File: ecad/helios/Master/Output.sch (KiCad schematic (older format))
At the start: 26 parts, among them J5 MCV 1,5/ 2-G-3,81, J6 MiniFit JR 5556 08A2, Q1 IRF9Z34NPbF, Q2 BSS84P, U2 STEF01FTR, U3 ISO7320FC, U4 UA9638

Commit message: Corrects anotation of Helios Master
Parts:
- D3, D4: value CPDT-5V0-HF -> CPDT-5V0USP-HF; Part Number CPDT-5V0-HF -> CPDT-5V0USP-HF
- renumbered R7 to R13, U4 to U7, U3 to U9
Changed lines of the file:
@@
 V36
 $Comp
-L master-rescue:ISO7320FC U3
+L master-rescue:ISO7320FC U9
 U 1 1 5AC3E36A
 P 2900 4100
-AR Path="/5AC39A79/5AC3E36A" Ref="U3"  Part="1"
+AR Path="/5AC39A79/5AC3E36A" Ref="U9"  Part="1"
 AR Path="/5AC440F9/5AC3E36A" Ref="U5"  Part="1"
 AR Path="/5AC443F1/5AC3E36A" Ref="U10"  Part="1"
 AR Path="/5AC443F5/5AC3E36A" Ref="U15"  Part="1"
-F 0 "U3" H 2900 4525 50  0000 C CNN
+F 0 "U9" H 2900 4525 50  0000 C CNN
 F 1 "ISO7320FC" H 2900 4450 50  0000 C CNN
 F 2 "Package_SO:SOIC-8_3.9x4.9mm_P1.27mm" H 2900 3750 50  0001 C CIN
@@
 $EndComp
 $Comp
-L master-rescue:UA9638 U4
+L master-rescue:UA9638 U7
 U 1 1 5AC3EEA4
 P 5750 4100
-AR Path="/5AC39A79/5AC3EEA4" Ref="U4"  Part="1"
+AR Path="/5AC39A79/5AC3EEA4" Ref="U7"  Part="1"
 AR Path="/5AC440F9/5AC3EEA4" Ref="U6"  Part="1"
 AR Path="/5AC443F1/5AC3EEA4" Ref="U11"  Part="1"
 AR Path="/5AC443F5/5AC3EEA4" Ref="U16"  Part="1"
-F 0 "U4" H 5600 4200 50  0000 C CNN
+F 0 "U7" H 5600 4200 50  0000 C CNN
 F 1 "UA9638" H 5650 4100 50  0000 C CNN
 F 2 "Package_SO:SOIC-8_3.9x4.9mm_P1.27mm" H 5750 4100 50  0001 C CNN
@@
 $EndComp
 $Comp
-L master-rescue:UA9638 U4
+L master-rescue:UA9638 U7
 U 2 1 5AC3EF24
 P 5750 5250
-AR Path="/5AC39A79/5AC3EF24" Ref="U4"  Part="2"
+AR Path="/5AC39A79/5AC3EF24" Ref="U7"  Part="2"
 AR Path="/5AC440F9/5AC3EF24" Ref="U6"  Part="2"
 AR Path="/5AC443F1/5AC3EF24" Ref="U11"  Part="2"
 AR Path="/5AC443F5/5AC3EF24" Ref="U16"  Part="2"
-F 0 "U4" H 5600 5350 50  0000 C CNN
+F 0 "U7" H 5600 5350 50  0000 C CNN
 F 1 "UA9638" H 5700 5250 50  0000 C CNN
 F 2 "Package_SO:SOIC-8_3.9x4.9mm_P1.27mm" H 5750 5250 50  0001 C CNN
@@
 $EndComp
 $Comp
-L master-rescue:R R7
+L master-rescue:R R13
 U 1 1 5B3E59CE
 P 10150 1850
-AR Path="/5AC39A79/5B3E59CE" Ref="R7"  Part="1"
+AR Path="/5AC39A79/5B3E59CE" Ref="R13"  Part="1"
 AR Path="/5AC440F9/5B3E59CE" Ref="R14"  Part="1"
 AR Path="/5AC443F1/5B3E59CE" Ref="R27"  Part="1"
 AR Path="/5AC443F5/5B3E59CE" Ref="R34"  Part="1"
-F 0 "R7" V 10230 1850 50  0000 C CNN
+F 0 "R13" V 10230 1850 50  0000 C CNN
 F 1 "10K" V 10150 1850 50  0000 C CNN
 F 2 "Resistor_SMD:R_0603_1608Metric" V 10080 1850 50  0001 C CNN
@@
 AR Path="/5AC443F1/5B3E9AF8" Ref="R26"  Part="1"
 AR Path="/5AC443F5/5B3E9AF8" Ref="R33"  Part="1"
-AR Path="/5AC39A79/5B3E9AF8" Ref="R6"  Part="1"
-F 0 "R6" V 8880 1800 50  0000 C CNN
+AR Path="/5AC39A79/5B3E9AF8" Ref="R12"  Part="1"
+F 0 "R12" V 8880 1800 50  0000 C CNN
 F 1 "100K" V 8800 1800 50  0000 C CNN
 F 2 "Resistor_SMD:R_0603_1608Metric" V 8730 1800 50  0001 C CNN
@@
 P 6850 4550
 F 0 "D3" H 6850 4766 50  0000 C CNN
-F 1 "CPDT-5V0-HF" H 6850 4675 50  0000 C CNN
+F 1 "CPDT-5V0USP-HF" H 6850 4675 50  0000 C CNN
 F 2 "Package_TO_SOT_SMD:SOT-23" H 6700 4550 50  0001 C CNN
 F 3 "~" H 6700 4550 50  0001 C CNN
-F 4 "CPDT-5V0-HF" H 6850 4550 50  0001 C CNN "Part Number"
+F 4 "CPDT-5V0USP-HF" H 6850 4550 50  0001 C CNN "Part Number"
 	1    6850 4550
 	1    0    0    -1
@@
 P 6850 5700
 F 0 "D4" H 6850 5916 50  0000 C CNN
-F 1 "CPDT-5V0-HF" H 6850 5825 50  0000 C CNN
+F 1 "CPDT-5V0USP-HF" H 6850 5825 50  0000 C CNN
 F 2 "Package_TO_SOT_SMD:SOT-23" H 6700 5700 50  0001 C CNN
 F 3 "~" H 6700 5700 50  0001 C CNN
-F 4 "CPDT-5V0-HF" H 6850 5700 50  0001 C CNN "Part Number"
+F 4 "CPDT-5V0USP-HF" H 6850 5700 50  0001 C CNN "Part Number"
 	1    6850 5700
 	1    0    0    -1

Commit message: Updates board for manufacturing
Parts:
- C2, C3: value 47uF, 50V -> (none)
- C45, C5, C6, C7: value 100nF -> 100n; Part Number 06035C104KAT2A -> CC0603KRX7R8BB104
- J6: value MiniFit JR 5556 08A2 -> MiniFit JR 5566 08A2
- Q1: footprint Package_TO_SOT_THT:TO-220-3_Horizontal_TabDown -> Package_TO_SOT_THT:TO-220-3_Vertical
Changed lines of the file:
@@
 F 0 "Q1" H 2600 1450 50  0000 L CNN
 F 1 "IRF9Z34NPbF" H 2600 1350 50  0000 L CNN
-F 2 "Package_TO_SOT_THT:TO-220-3_Horizontal_TabDown" H 2600 1500 50  0001 C CNN
+F 2 "Package_TO_SOT_THT:TO-220-3_Vertical" H 2600 1500 50  0001 C CNN
 F 3 "" H 2400 1400 50  0001 C CNN
 F 4 "IRF9Z34NPbF" H 2400 1400 60  0001 C CNN "Part Number"
@@
 AR Path="/5AC443F5/5AC3EBB4" Ref="C29"  Part="1"
 F 0 "C7" H 3575 3900 50  0000 L CNN
-F 1 "100nF" H 3575 3700 50  0000 L CNN
+F 1 "100n" H 3575 3700 50  0000 L CNN
 F 2 "Capacitor_SMD:C_0603_1608Metric" H 3588 3650 50  0001 C CNN
 F 3 "" H 3550 3800 50  0001 C CNN
-F 4 "06035C104KAT2A" H 3550 3800 60  0001 C CNN "Part Number"
+F 4 "CC0603KRX7R8BB104" H 3550 3800 60  0001 C CNN "Part Number"
 	1    3550 3800
 	1    0    0    -1
@@
 AR Path="/5AC443F5/5AC3EDD3" Ref="C28"  Part="1"
 F 0 "C6" H 1775 3850 50  0000 L CNN
-F 1 "100nF" H 1775 3650 50  0000 L CNN
+F 1 "100n" H 1775 3650 50  0000 L CNN
 F 2 "Capacitor_SMD:C_0603_1608Metric" H 1788 3600 50  0001 C CNN
 F 3 "" H 1750 3750 50  0001 C CNN
-F 4 "06035C104KAT2A" H 1750 3750 60  0001 C CNN "Part Number"
+F 4 "CC0603KRX7R8BB104" H 1750 3750 60  0001 C CNN "Part Number"
 	1    1750 3750
 	1    0    0    -1
@@
 AR Path="/5AC443F5/5AC3FC48" Ref="J10"  Part="1"
 F 0 "J6" H 9600 4400 50  0000 C CNN
-F 1 "MiniFit JR 5556 08A2" H 9600 3900 50  0000 C CNN
+F 1 "MiniFit JR 5566 08A2" H 9600 3900 50  0000 C CNN
 F 2 "FORT:Molex_MiniFit-JR-5556-08A_2x04x4.20mm_Straight" H 9550 4200 50  0001 C CNN
 F 3 "" H 9550 4200 50  0001 C CNN
@@
 AR Path="/5AC443F5/5AC420D7" Ref="C27"  Part="1"
 F 0 "C5" H 6125 3450 50  0000 L CNN
-F 1 "100nF" H 6125 3250 50  0000 L CNN
+F 1 "100n" H 6125 3250 50  0000 L CNN
 F 2 "Capacitor_SMD:C_0603_1608Metric" H 6138 3200 50  0001 C CNN
 F 3 "" H 6100 3350 50  0001 C CNN
-F 4 "06035C104KAT2A" H 6100 3350 60  0001 C CNN "Part Number"
+F 4 "CC0603KRX7R8BB104" H 6100 3350 60  0001 C CNN "Part Number"
 	1    6100 3350
 	1    0    0    -1
@@
 AR Path="/5AC443F5/5B3E77BC" Ref="C55"  Part="1"
 F 0 "C3" H 10575 1900 50  0000 L CNN
-F 1 "47uF, 50V" H 10575 1700 50  0000 L CNN
+F 1 "                                                                                                                                                                                                                                                                                                                                                                                                                                                                                                                                                                                                                                                                                                                               " H 10575 1700 50  0000 L CNN
 F 2 "Capacitor_SMD:CP_Elec_6.3x7.7" H 10588 1650 50  0001 C CNN
 F 3 "" H 10550 1800 50  0001 C CNN
@@
 AR Path="/5AC443F5/5B3E7AB8" Ref="C54"  Part="1"
 F 0 "C2" H 5975 1800 50  0000 L CNN
-F 1 "47uF, 50V" H 5975 1600 50  0000 L CNN
+F 1 "                                                                                                                                                                                                                                                                                                                                                                                                                                                                                                                                                                                                                                                                                                                               " H 5975 1600 50  0000 L CNN
 F 2 "Capacitor_SMD:CP_Elec_6.3x7.7" H 5988 1550 50  0001 C CNN
 F 3 "" H 5950 1700 50  0001 C CNN
@@
 AR Path="/5AC39A79/5B3E7E16" Ref="C1"  Part="1"
 F 0 "C1" H 5675 1800 50  0000 L CNN
-F 1 "100nF" H 5675 1600 50  0000 L CNN
+F 1 "100n" H 5675 1600 50  0000 L CNN
 F 2 "Capacitor_SMD:C_0603_1608Metric" H 5688 1550 50  0001 C CNN
 F 3 "" H 5650 1700 50  0001 C CNN
-F 4 "06035C104KAT2A" H 5650 1700 60  0001 C CNN "Part Number"
+F 4 "CC0603KRX7R8BB104" H 5650 1700 60  0001 C CNN "Part Number"
 	1    5650 1700
 	1    0    0    -1

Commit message: Makes all electronics production ready
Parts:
- removed D3, D4: CPDT-5V0USP-HF, Package_TO_SOT_SMD:SOT-23, symbol Device:D_TVS_x2_AAC
- added D3, D4: SP1002-02TG, Package_TO_SOT_SMD:SOT-353_SC-70-5, symbol fort:SP1002-02TG
- added R21: 51, Resistor_SMD:R_0603_1608Metric, symbol master-rescue:R
- C2, C3: value (none) -> 47uF
- C45, C5, C6, C7: Part Number CC0603KRX7R8BB104 -> GPC0603104
- R2: value 249K -> 270k; Part Number RMCF0603FT249K -> GPR0603270k
- R3: value 25.5 -> 51; Part Number RMCF0603FT25R5 -> GPR060351
- R4: value 412K -> 390k; Part Number RMCF0603FT412K -> GPC0603390k
- R9: value 604 -> 1k; Part Number RMCF0603FT604R -> GPC06031k
- U7: Part Number UA9638CDR -> UA9638
- U7: Part Number (none) -> UA9638
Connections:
- wire segments 160 -> 168

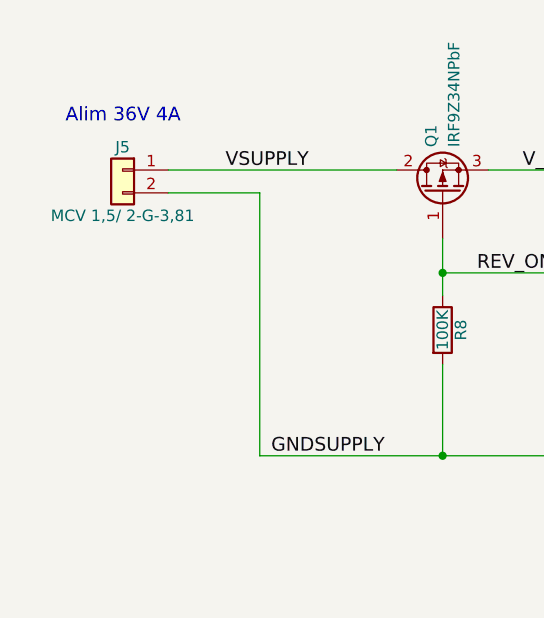
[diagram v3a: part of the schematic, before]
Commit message: Updates Helios Master 36V power Connector
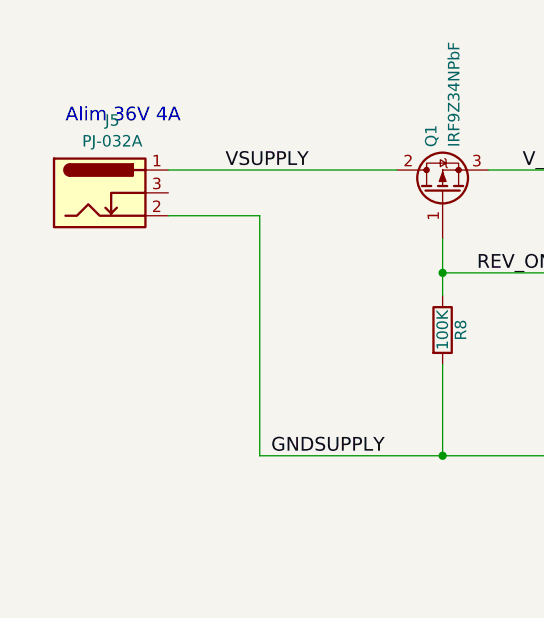
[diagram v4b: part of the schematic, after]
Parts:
- removed J5: MCV 1,5/ 2-G-3,81, Connector_Phoenix_MC:PhoenixContact_MCV_1,5_2-G-3.81_1x02_P3.81mm_Vertical, symbol master-rescue:Conn_01x02
- added J5: PJ-032A, FORT:PJ-032A, symbol Connector:Barrel_Jack_Switch
- R9: Part Number GPC06031k -> GPR06031K
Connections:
- net GNDSUPPLY: now also J5.2
- net VSUPPLY: now also J5.1
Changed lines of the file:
@@
 $EndDescr
-$Comp
-L master-rescue:Conn_01x02 J5
-U 1 1 5AC39A82
-P 1000 1300
-AR Path="/5AC39A79/5AC39A82" Ref="J5"  Part="1"
-AR Path="/5AC440F9/5AC39A82" Ref="J5"  Part="1"
-AR Path="/5AC443F1/5AC39A82" Ref="J7"  Part="1"
-AR Path="/5AC443F5/5AC39A82" Ref="J9"  Part="1"
-F 0 "J5" H 1000 1400 50  0000 C CNN
-F 1 "MCV 1,5/ 2-G-3,81" H 1000 1100 50  0000 C CNN
-F 2 "Connector_Phoenix_MC:PhoenixContact_MCV_1,5_2-G-3.81_1x02_P3.81mm_Vertical" H 1000 1300 50  0001 C CNN
-F 3 "" H 1000 1300 50  0001 C CNN
-F 4 "1803426" H 1000 1300 60  0001 C CNN "Part Number"
-	1    1000 1300
-	-1   0    0    -1
-$EndComp
 $Comp
 L master-rescue:Q_PMOS_GDS Q1
@@
 F 2 "Resistor_SMD:R_0603_1608Metric" V 9380 2150 50  0001 C CNN
 F 3 "" H 9450 2150 50  0001 C CNN
-F 4 "GPC06031k" H 9450 2150 60  0001 C CNN "Part Number"
+F 4 "GPR06031K" H 9450 2150 60  0001 C CNN "Part Number"
 	1    9450 2150
 	1    0    0    -1
@@
 	6400 5450 7300 5450
 Wire Wire Line
-	1600 1400 1600 2550
+	1600 1500 1600 2550
 Wire Wire Line
 	1600 2550 2400 2550
 Wire Wire Line
-	1200 1400 1600 1400
+	1200 1500 1600 1500
 Connection ~ 2400 2550
+$Comp
+L Connector:Barrel_Jack_Switch J5
+U 1 1 5CDFC12E
+P 900 1400
+F 0 "J5" H 955 1717 50  0000 C CNN
+F 1 "PJ-032A" H 955 1626 50  0000 C CNN
+F 2 "FORT:PJ-032A" H 950 1360 50  0001 C CNN
+F 3 "~" H 950 1360 50  0001 C CNN
+F 4 "PJ-032A" H 900 1400 50  0001 C CNN "Part Number"
+	1    900  1400
+	1    0    0    -1
+$EndComp
 $EndSCHEMATC
